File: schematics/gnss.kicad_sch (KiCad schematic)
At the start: 1 part, among them IC1 TESEO-LIV3R

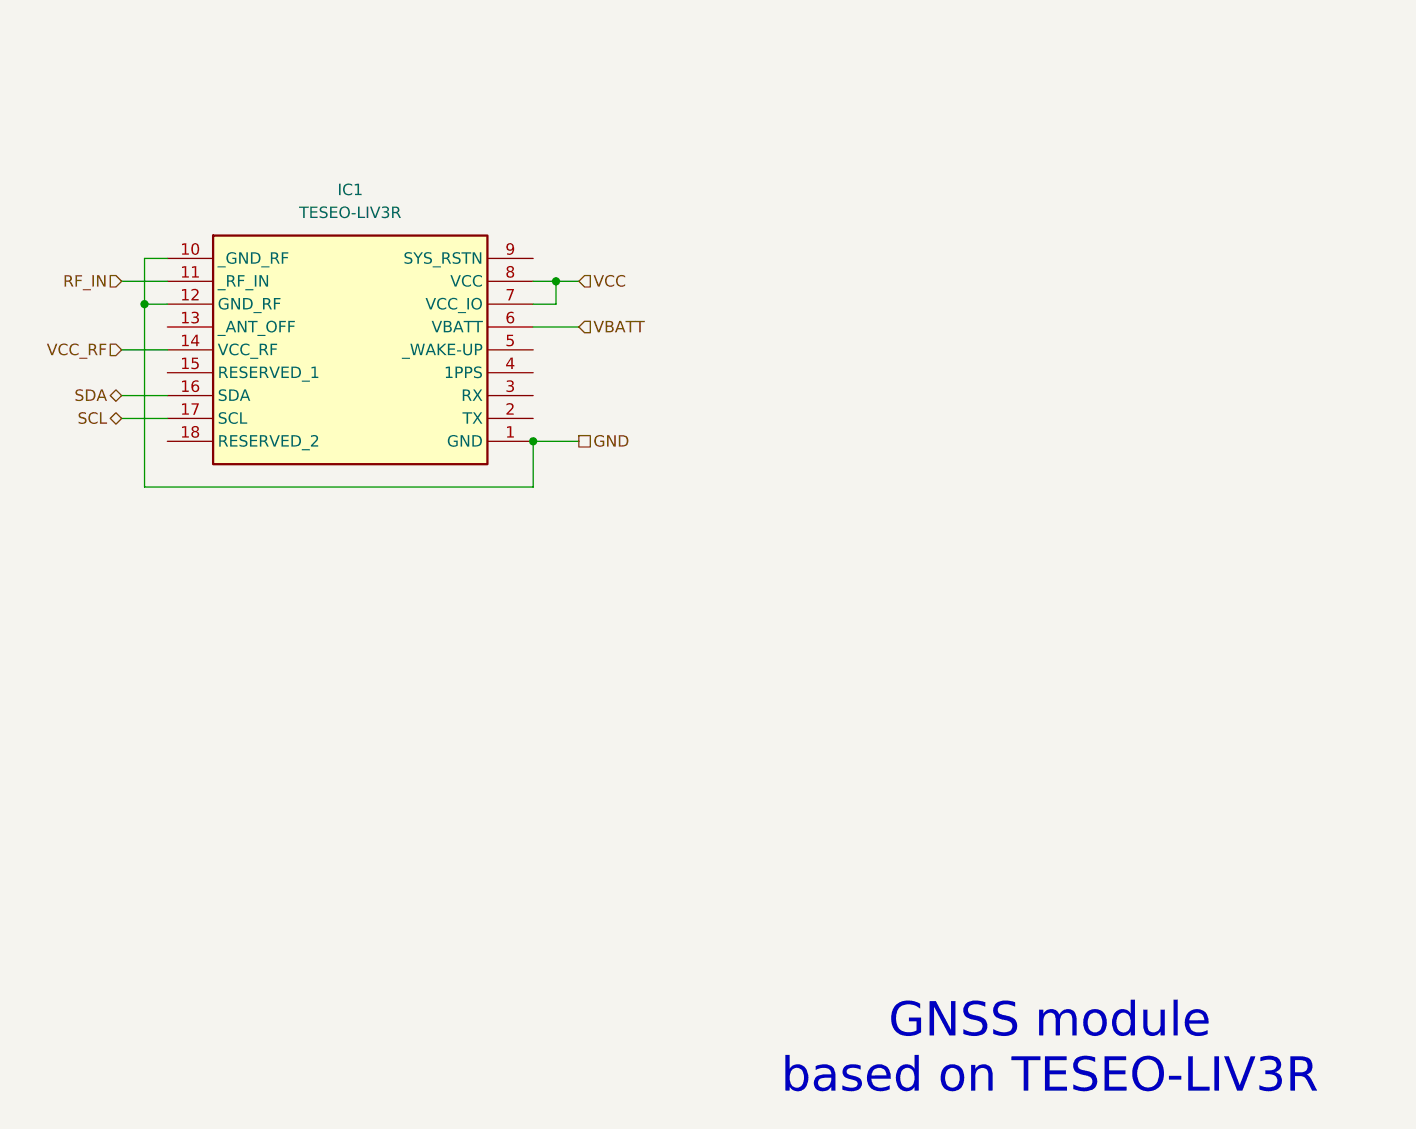
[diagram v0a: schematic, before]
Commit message: Normalized sheet titles; added MMCX connector for GPS antenna + active antenna power switch
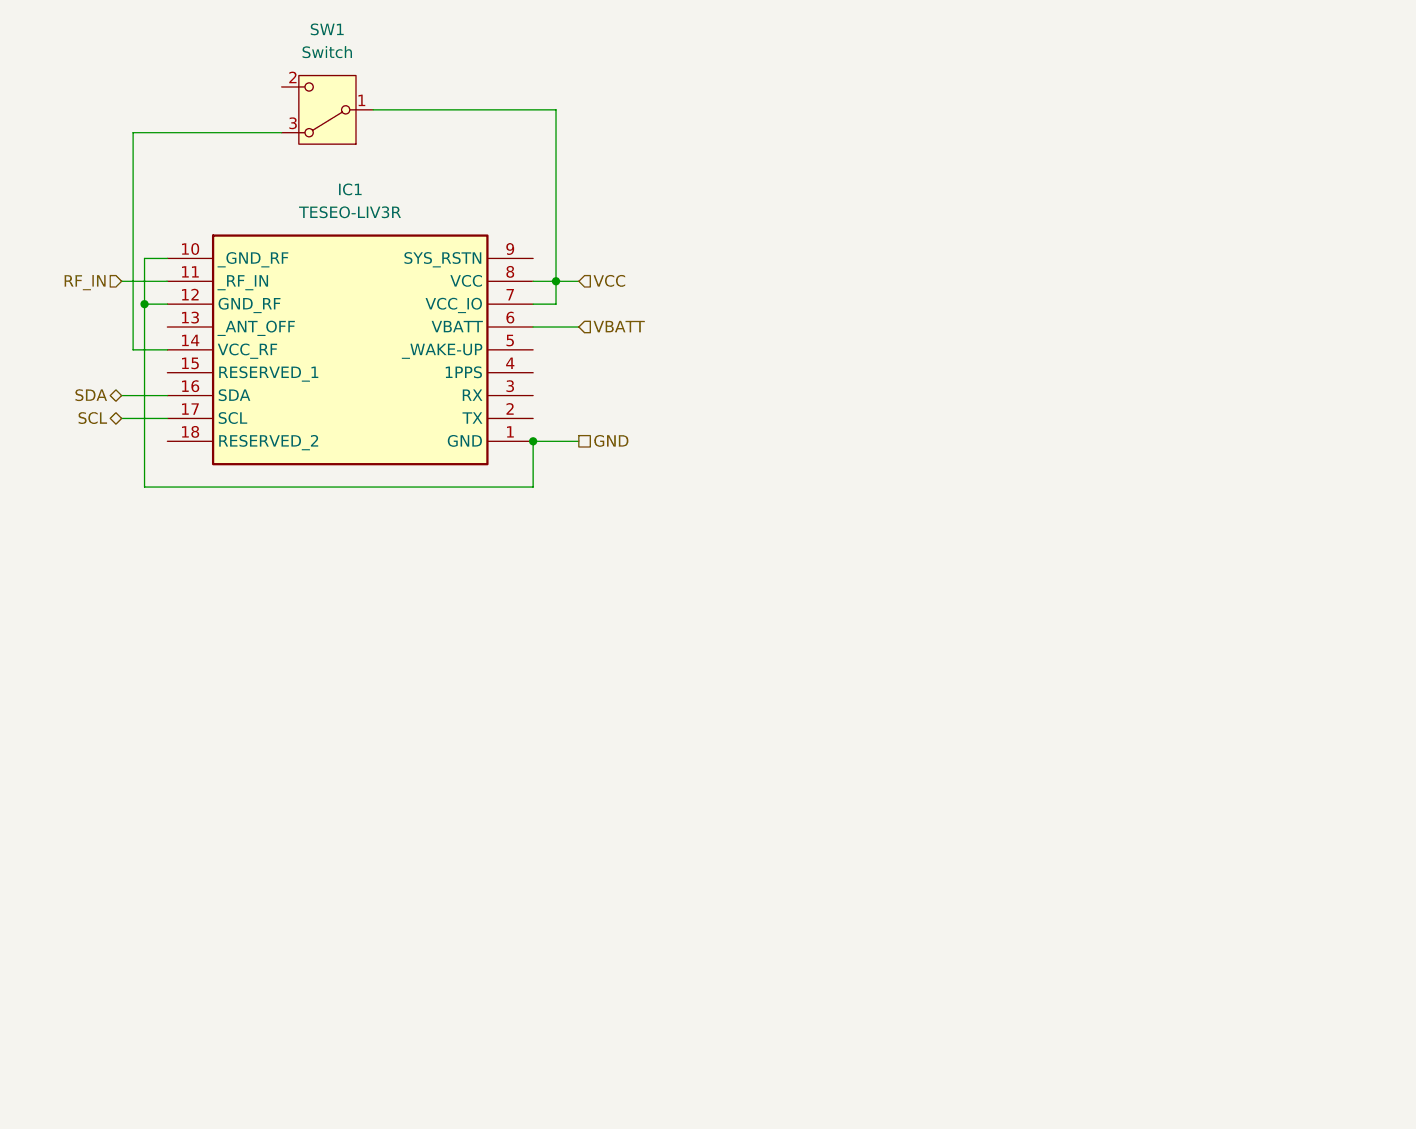
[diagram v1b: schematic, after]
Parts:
- added SW1: Switch, Button_Switch_THT:SW_Slide-03_Wuerth-WS-SLTV_10x2.5x6.4_P2.54mm, symbol Switch:SW_Wuerth_450301014042
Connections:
- net VCC: now also SW1.1 (B)
- net VCC_RF: no longer names the net of IC1.14 (VCC_RF)
- net VCC_RF: now also SW1.3 (A)
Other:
- note removed: "GNSS module based on TESEO-LIV3R"
- title: (none) -> GNSS module based on TESEO-LIV3R
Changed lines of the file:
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@@
 	(generator_version "9.0")
 	(paper "A4")
-	(text "GNSS module\nbased on TESEO-LIV3R"
-		(exclude_from_sim no)
-		(at 226.314 174.244 0)
-		(effects
-			(font
-				(size 3.81 3.81)
-			)
-		)
+	(title_block
+		(title "GNSS module based on TESEO-LIV3R")
+		(comment 1 "The switch enables active GNSS antennas VCC")
 	)
 	(junction
@@
 	(wire
 		(pts
+			(xy 124.46 96.52) (xy 124.46 72.39)
+		)
+		(stroke
+			(width 0)
+			(type default)
+		)
+	)
+	(wire
+		(pts
 			(xy 125.73 111.76) (xy 168.91 111.76)
 		)
@@
 	(wire
 		(pts
+			(xy 171.45 69.85) (xy 171.45 88.9)
+		)
+		(stroke
+			(width 0)
+			(type default)
+		)
+	)
+	(wire
+		(pts
+			(xy 124.46 72.39) (xy 140.97 72.39)
+		)
+		(stroke
+			(width 0)
+			(type default)
+		)
+	)
+	(wire
+		(pts
 			(xy 173.99 106.68) (xy 168.91 106.68)
 		)
@@
 	(wire
 		(pts
+			(xy 128.27 96.52) (xy 124.46 96.52)
+		)
+		(stroke
+			(width 0)
+			(type default)
+		)
+	)
+	(wire
+		(pts
 			(xy 173.99 88.9) (xy 171.45 88.9)
 		)
@@
 	(wire
 		(pts
+			(xy 151.13 69.85) (xy 171.45 69.85)
+		)
+		(stroke
+			(width 0)
+			(type default)
+		)
+	)
+	(wire
+		(pts
 			(xy 171.45 88.9) (xy 168.91 88.9)
 		)
@@
 		(pts
 			(xy 125.73 86.36) (xy 125.73 91.44)
-		)
-		(stroke
-			(width 0)
-			(type default)
-		)
-	)
-	(wire
-		(pts
-			(xy 123.19 96.52) (xy 128.27 96.52)
 		)
 		(stroke
@@
 		)
 	)
-	(hierarchical_label "VCC_RF"
-		(shape input)
-		(at 123.19 96.52 180)
-		(effects
-			(font
-				(size 1.27 1.27)
-			)
-			(justify right)
-		)
-	)
 	(hierarchical_label "GND"
 		(shape passive)
@@
 		)
 	)
+	(symbol
+		(lib_id "Switch:SW_Wuerth_450301014042")
+		(at 146.05 69.85 180)
+		(unit 1)
+		(exclude_from_sim no)
+		(in_bom yes)
+		(on_board yes)
+		(dnp no)
+		(fields_autoplaced yes)
+		(property "Reference" "SW1"
+			(at 146.05 60.96 0)
+			(effects
+				(font
+					(size 1.27 1.27)
+				)
+			)
+		)
+		(property "Value" "Switch"
+			(at 146.05 63.5 0)
+			(effects
+				(font
+					(size 1.27 1.27)
+				)
+			)
+		)
+		(property "Footprint" "Button_Switch_THT:SW_Slide-03_Wuerth-WS-SLTV_10x2.5x6.4_P2.54mm"
+			(at 146.05 59.69 0)
+			(effects
+				(font
+					(size 1.27 1.27)
+				)
+				(hide yes)
+			)
+		)
+		(property "Datasheet" "https://www.we-online.com/components/products/datasheet/450301014042.pdf"
+			(at 146.05 62.23 0)
+			(effects
+				(font
+					(size 1.27 1.27)
+				)
+				(hide yes)
+			)
+		)
+		(property "Description" "Switch slide, single pole double throw"
+			(at 146.05 69.85 0)
+			(effects
+				(font
+					(size 1.27 1.27)
+				)
+				(hide yes)
+			)
+		)
+		(pin "3"
+		)
+		(pin "1"
+		)
+		(pin "2"
+		)
+		(instances
+			(project "bike-sensors-logger"
+				(path "/2c1d9222-af16-428b-85a5-a3d420373d70/20b38507-7c11-47bc-b74f-fc37e2ef1b90"
+					(reference "SW1")
+					(unit 1)
+				)
+			)
+		)
+	)

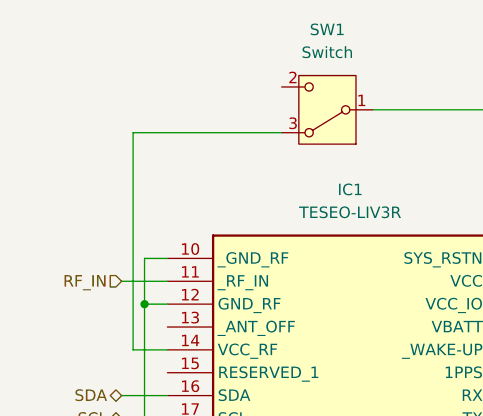
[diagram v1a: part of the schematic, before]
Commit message: Added ANT_PWR pin to signal the GNSS switch's state (TODO: link to a status LED)
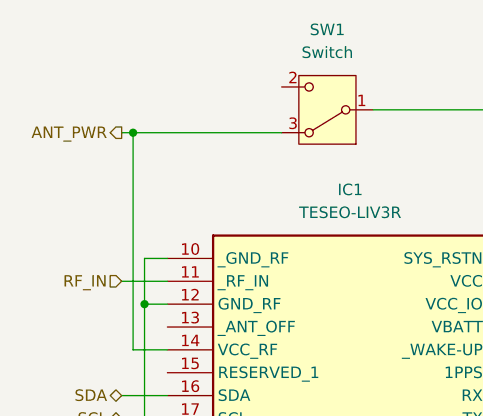
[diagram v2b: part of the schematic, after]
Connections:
- net ANT_PWR: now reaches IC1.14 (VCC_RF), SW1.3 (A)
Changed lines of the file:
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@@
+	)
+	(junction
+		(at 124.46 72.39)
+		(diameter 0)
+		(color 0 0 0 0)
 	)
 	(junction
@@
 		(pts
 			(xy 124.46 72.39) (xy 140.97 72.39)
+		)
+		(stroke
+			(width 0)
+			(type default)
+		)
+	)
+	(wire
+		(pts
+			(xy 123.19 72.39) (xy 124.46 72.39)
 		)
 		(stroke
@@
 		)
 	)
+	(hierarchical_label "ANT_PWR"
+		(shape output)
+		(at 123.19 72.39 180)
+		(effects
+			(font
+				(size 1.27 1.27)
+			)
+			(justify right)
+		)
+	)

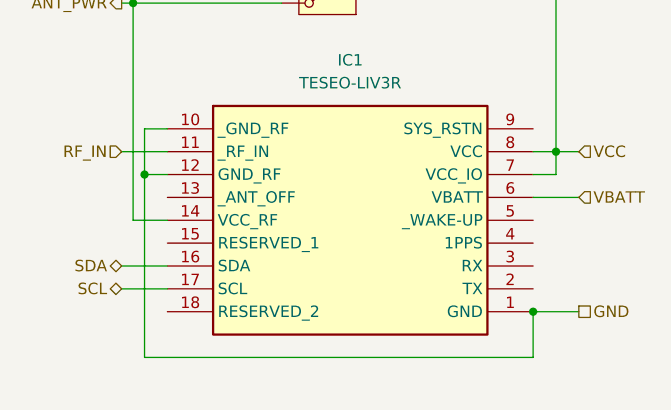
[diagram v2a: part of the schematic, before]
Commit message: Include GND in each schema sub-pages
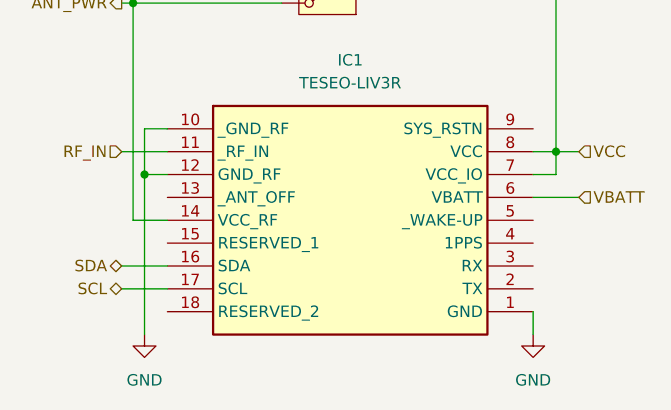
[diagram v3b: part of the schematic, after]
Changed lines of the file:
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@@
 		(color 0 0 0 0)
 	)
-	(junction
-		(at 168.91 106.68)
-		(diameter 0)
-		(color 0 0 0 0)
-	)
 	(wire
 		(pts
@@
 	(wire
 		(pts
-			(xy 125.73 111.76) (xy 168.91 111.76)
-		)
-		(stroke
-			(width 0)
-			(type default)
-		)
-	)
-	(wire
-		(pts
 			(xy 171.45 69.85) (xy 171.45 88.9)
 		)
@@
 	(wire
 		(pts
-			(xy 173.99 106.68) (xy 168.91 106.68)
-		)
-		(stroke
-			(width 0)
-			(type default)
-		)
-	)
-	(wire
-		(pts
 			(xy 171.45 91.44) (xy 171.45 88.9)
 		)
@@
 	(wire
 		(pts
-			(xy 168.91 106.68) (xy 168.91 111.76)
+			(xy 168.91 106.68) (xy 168.91 109.22)
 		)
 		(stroke
@@
 	(wire
 		(pts
-			(xy 125.73 91.44) (xy 125.73 111.76)
+			(xy 125.73 91.44) (xy 125.73 109.22)
 		)
 		(stroke
@@
 			)
 			(justify right)
-		)
-	)
-	(hierarchical_label "GND"
-		(shape passive)
-		(at 173.99 106.68 0)
-		(effects
-			(font
-				(size 1.27 1.27)
-			)
-			(justify left)
 		)
 	)
@@
 					(unit 1)
 				)
+			)
+		)
+	)
+	(symbol
+		(lib_id "power:GND")
+		(at 168.91 109.22 0)
+		(unit 1)
+		(exclude_from_sim no)
+		(in_bom yes)
+		(on_board yes)
+		(dnp no)
+		(fields_autoplaced yes)
+		(property "Reference" "#PWR016"
+			(at 168.91 115.57 0)
+			(effects
+				(font
+					(size 1.27 1.27)
+				)
+				(hide yes)
+			)
+		)
+		(property "Value" "GND"
+			(at 168.91 114.3 0)
+			(effects
+				(font
+					(size 1.27 1.27)
+				)
+			)
+		)
+		(property "Footprint" ""
+			(at 168.91 109.22 0)
+			(effects
+				(font
+					(size 1.27 1.27)
+				)
+				(hide yes)
+			)
+		)
+		(property "Datasheet" ""
+			(at 168.91 109.22 0)
+			(effects
+				(font
+					(size 1.27 1.27)
+				)
+				(hide yes)
+			)
+		)
+		(property "Description" "Power symbol creates a global label with name \"GND\" , ground"
+			(at 168.91 109.22 0)
+			(effects
+				(font
+					(size 1.27 1.27)
+				)
+				(hide yes)
+			)
+		)
+		(pin "1"
+		)
+		(instances
+			(project "bike-sensors-logger"
+				(path "/2c1d9222-af16-428b-85a5-a3d420373d70/20b38507-7c11-47bc-b74f-fc37e2ef1b90"
+					(reference "#PWR016")
+					(unit 1)
+				)
+			)
+		)
+	)
+	(symbol
+		(lib_id "power:GND")
+		(at 125.73 109.22 0)
+		(unit 1)
+		(exclude_from_sim no)
+		(in_bom yes)
+		(on_board yes)
+		(dnp no)
+		(fields_autoplaced yes)
+		(property "Reference" "#PWR03"
+			(at 125.73 115.57 0)
+			(effects
+				(font
+					(size 1.27 1.27)
+				)
+				(hide yes)
+			)
+		)
+		(property "Value" "GND"
+			(at 125.73 114.3 0)
+			(effects
+				(font
+					(size 1.27 1.27)
+				)
+			)
+		)
+		(property "Footprint" ""
+			(at 125.73 109.22 0)
+			(effects
+				(font
+					(size 1.27 1.27)
+				)
+				(hide yes)
+			)
+		)
+		(property "Datasheet" ""
+			(at 125.73 109.22 0)
+			(effects
+				(font
+					(size 1.27 1.27)
+				)
+				(hide yes)
+			)
+		)
+		(property "Description" "Power symbol creates a global label with name \"GND\" , ground"
+			(at 125.73 109.22 0)
+			(effects
+				(font
+					(size 1.27 1.27)
+				)
+				(hide yes)
+			)
+		)
+		(pin "1"
+		)
+		(instances
+			(project "bike-sensors-logger"
+				(path "/2c1d9222-af16-428b-85a5-a3d420373d70/20b38507-7c11-47bc-b74f-fc37e2ef1b90"
+					(reference "#PWR03")
+					(unit 1)
+				)
